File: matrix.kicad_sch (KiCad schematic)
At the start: 2 parts

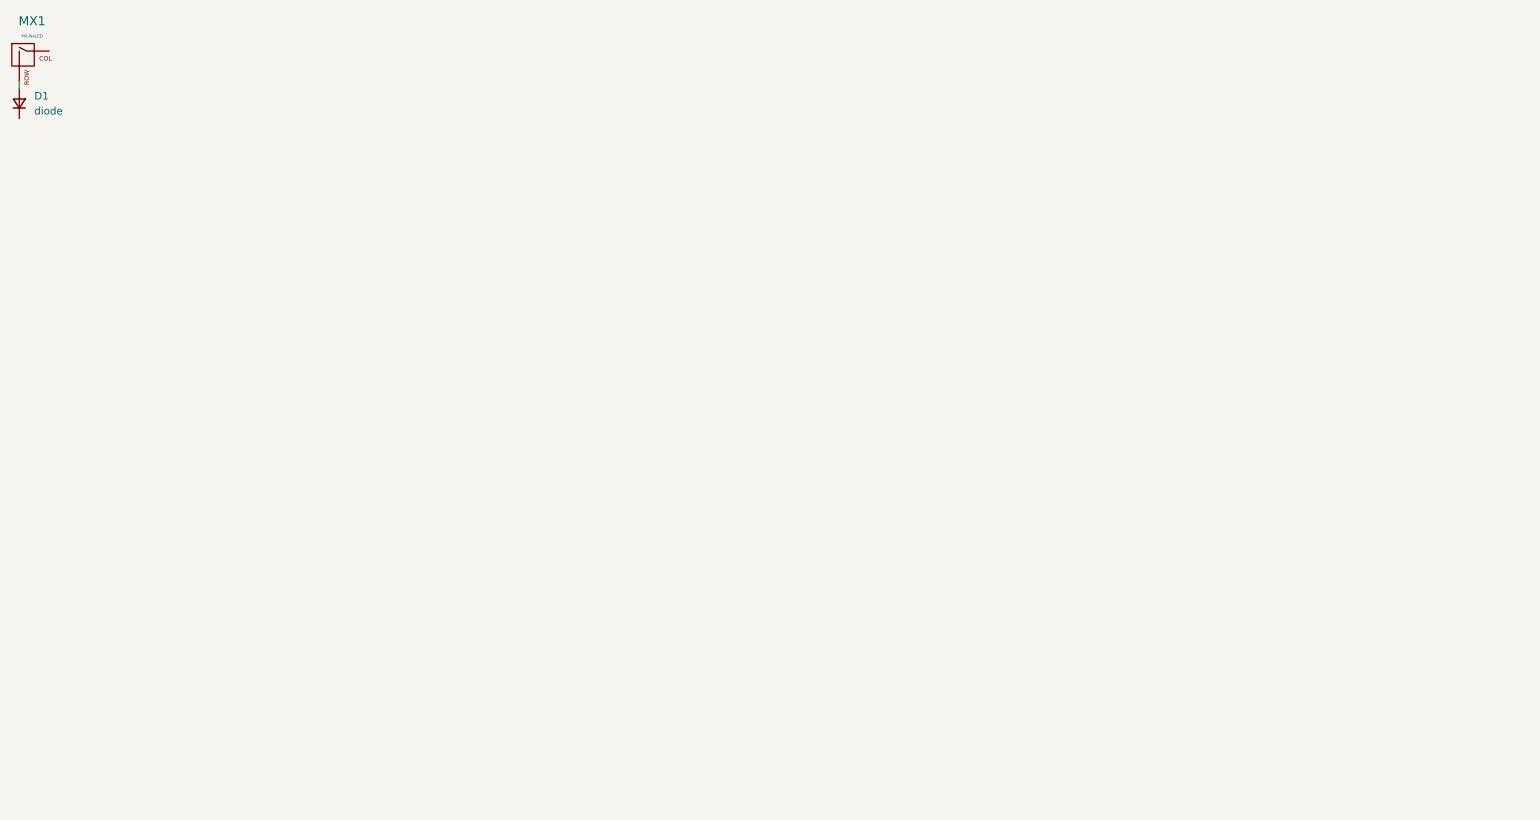
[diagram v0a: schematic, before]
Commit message: First version of schematic, including duplex matrix.
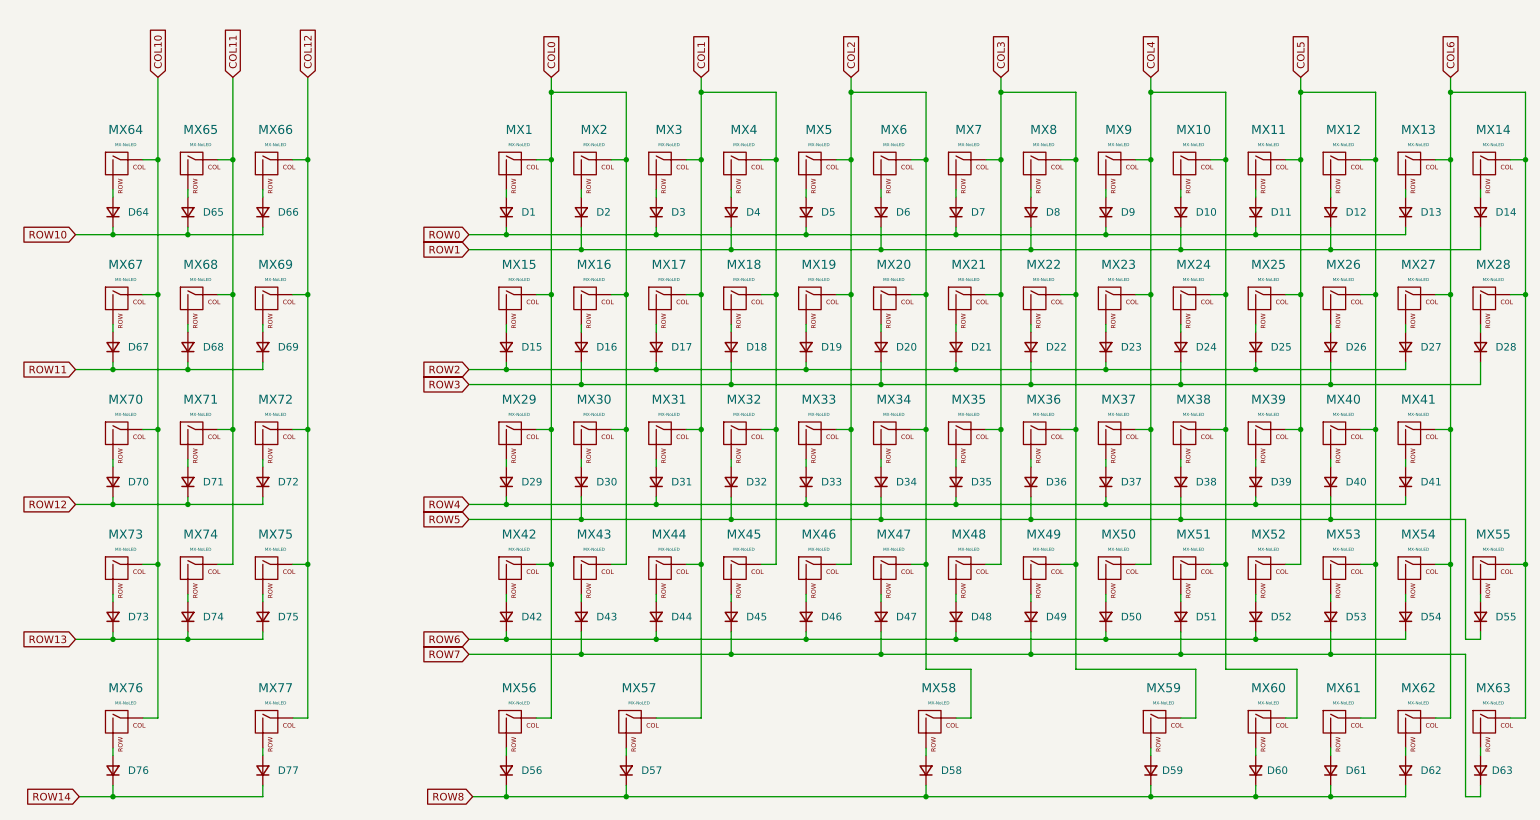
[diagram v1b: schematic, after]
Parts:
- added D10, D11, D12, D13, D14, D15, D16, D17, D18, D19, D2, D20, D21, D22, D23, D24, D25, D26, D27, D28, D29, D3, D30, D31, D32, D33, D34, D35, D36, D37, D38, D39, D4, D40, D41, D42, D43, D44, D45, D46, D47, D48, D49, D5, D50, D51, D52, D53, D54, D55, D56, D57, D58, D59, D6, D60, D61, D62, D63, D64, D65, D66, D67, D68, D69, D7, D70, D71, D72, D73, D74, D75, D76, D77, D8, D9: ~, symbol Device:D_Small
- added MX10, MX11, MX12, MX13, MX14, MX15, MX16, MX17, MX18, MX19, MX2, MX20, MX21, MX22, MX23, MX24, MX25, MX26, MX27, MX28, MX29, MX3, MX30, MX31, MX32, MX33, MX34, MX35, MX36, MX37, MX38, MX39, MX4, MX40, MX41, MX42, MX43, MX44, MX45, MX46, MX47, MX48, MX49, MX5, MX50, MX51, MX52, MX53, MX54, MX55, MX56, MX57, MX58, MX59, MX6, MX60, MX61, MX62, MX63, MX64, MX65, MX66, MX67, MX68, MX69, MX7, MX70, MX71, MX72, MX73, MX74, MX75, MX76, MX77, MX8, MX9: MX-NoLED, symbol MX_Alps_Hybrid:MX-NoLED
- D1: value diode -> ~
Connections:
- net ROW0: now reaches D1.1 (K)
- net ROW0: now also D11.1 (K), D13.1 (K), D3.1 (K), D5.1 (K), D7.1 (K), D9.1 (K)
- net COL0: now reaches MX1.1 (COL)
- net COL0: now also MX15.1 (COL), MX16.1 (COL), MX2.1 (COL), MX29.1 (COL), MX30.1 (COL), MX42.1 (COL), MX43.1 (COL), MX56.1 (COL)
- new net: D65.2 (A), MX65.2 (ROW)
- new net: D21.2 (A), MX21.2 (ROW)
- new net: D74.2 (A), MX74.2 (ROW)
- new net: D17.2 (A), MX17.2 (ROW)
- new net: D15.2 (A), MX15.2 (ROW)
- new net: D49.2 (A), MX49.2 (ROW)
- new net: D51.2 (A), MX51.2 (ROW)
- new net: D20.2 (A), MX20.2 (ROW)
- new net: D18.2 (A), MX18.2 (ROW)
- new net: D26.2 (A), MX26.2 (ROW)
- new net: D64.2 (A), MX64.2 (ROW)
- new net: D24.2 (A), MX24.2 (ROW)
- new net: D67.2 (A), MX67.2 (ROW)
- new net: D34.2 (A), MX34.2 (ROW)
- new net: D25.2 (A), MX25.2 (ROW)
- new net: D59.2 (A), MX59.2 (ROW)
- new net: D73.2 (A), MX73.2 (ROW)
- new net: D44.2 (A), MX44.2 (ROW)
- new net: D39.2 (A), MX39.2 (ROW)
- new net: D37.2 (A), MX37.2 (ROW)
- new net: D10.2 (A), MX10.2 (ROW)
- new net: D48.2 (A), MX48.2 (ROW)
- new net: D76.2 (A), MX76.2 (ROW)
- new net: D68.2 (A), MX68.2 (ROW)
- new net: D33.2 (A), MX33.2 (ROW)
- new net: D66.2 (A), MX66.2 (ROW)
- new net: D22.2 (A), MX22.2 (ROW)
- new net: D5.2 (A), MX5.2 (ROW)
- new net: D3.2 (A), MX3.2 (ROW)
- new net: D6.2 (A), MX6.2 (ROW)
- new net: D63.2 (A), MX63.2 (ROW)
- new net: D40.2 (A), MX40.2 (ROW)
- new net: D50.2 (A), MX50.2 (ROW)
- new net: D19.2 (A), MX19.2 (ROW)
- new net: D31.2 (A), MX31.2 (ROW)
- new net: D52.2 (A), MX52.2 (ROW)
- new net: D28.2 (A), MX28.2 (ROW)
- new net: D47.2 (A), MX47.2 (ROW)
- new net: D30.2 (A), MX30.2 (ROW)
- new net: D53.2 (A), MX53.2 (ROW)
- new net: D13.2 (A), MX13.2 (ROW)
- new net: D42.2 (A), MX42.2 (ROW)
- new net: D72.2 (A), MX72.2 (ROW)
- new net: D12.2 (A), MX12.2 (ROW)
- new net: D2.2 (A), MX2.2 (ROW)
- new net: D23.2 (A), MX23.2 (ROW)
- new net: D56.2 (A), MX56.2 (ROW)
- new net: D9.2 (A), MX9.2 (ROW)
- new net: D14.2 (A), MX14.2 (ROW)
- new net: D11.2 (A), MX11.2 (ROW)
- new net: D8.2 (A), MX8.2 (ROW)
- new net: D35.2 (A), MX35.2 (ROW)
- new net: D29.2 (A), MX29.2 (ROW)
- new net: D45.2 (A), MX45.2 (ROW)
- new net: D46.2 (A), MX46.2 (ROW)
- new net: D7.2 (A), MX7.2 (ROW)
- new net: D16.2 (A), MX16.2 (ROW)
- new net: D57.2 (A), MX57.2 (ROW)
- new net: D58.2 (A), MX58.2 (ROW)
- new net: D36.2 (A), MX36.2 (ROW)
- new net: D75.2 (A), MX75.2 (ROW)
- new net: D41.2 (A), MX41.2 (ROW)
- new net: D54.2 (A), MX54.2 (ROW)
- new net: D60.2 (A), MX60.2 (ROW)
- new net: D32.2 (A), MX32.2 (ROW)
- new net: D55.2 (A), MX55.2 (ROW)
- new net: D69.2 (A), MX69.2 (ROW)
- new net: D4.2 (A), MX4.2 (ROW)
- new net: D43.2 (A), MX43.2 (ROW)
- new net: D71.2 (A), MX71.2 (ROW)
- new net: D62.2 (A), MX62.2 (ROW)
- new net: D61.2 (A), MX61.2 (ROW)
- new net: D77.2 (A), MX77.2 (ROW)
- new net: D38.2 (A), MX38.2 (ROW)
- new net: D70.2 (A), MX70.2 (ROW)
- new net: D27.2 (A), MX27.2 (ROW)
- new net COL1: MX17.1 (COL), MX18.1 (COL), MX3.1 (COL), MX31.1 (COL), MX32.1 (COL), MX4.1 (COL), MX44.1 (COL), MX45.1 (COL), MX57.1 (COL)
- new net COL10: MX64.1 (COL), MX67.1 (COL), MX70.1 (COL), MX73.1 (COL), MX76.1 (COL)
- new net COL11: MX65.1 (COL), MX68.1 (COL), MX71.1 (COL), MX74.1 (COL)
- new net COL12: MX66.1 (COL), MX69.1 (COL), MX72.1 (COL), MX75.1 (COL), MX77.1 (COL)
- new net COL2: MX19.1 (COL), MX20.1 (COL), MX33.1 (COL), MX34.1 (COL), MX46.1 (COL), MX47.1 (COL), MX5.1 (COL), MX58.1 (COL), MX6.1 (COL)
- new net COL3: MX21.1 (COL), MX22.1 (COL), MX35.1 (COL), MX36.1 (COL), MX48.1 (COL), MX49.1 (COL), MX59.1 (COL), MX7.1 (COL), MX8.1 (COL)
- new net COL4: MX10.1 (COL), MX23.1 (COL), MX24.1 (COL), MX37.1 (COL), MX38.1 (COL), MX50.1 (COL), MX51.1 (COL), MX60.1 (COL), MX9.1 (COL)
- new net COL5: MX11.1 (COL), MX12.1 (COL), MX25.1 (COL), MX26.1 (COL), MX39.1 (COL), MX40.1 (COL), MX52.1 (COL), MX53.1 (COL), MX61.1 (COL)
- new net COL6: MX13.1 (COL), MX14.1 (COL), MX27.1 (COL), MX28.1 (COL), MX41.1 (COL), MX54.1 (COL), MX55.1 (COL), MX62.1 (COL), MX63.1 (COL)
- new net ROW1: D10.1 (K), D12.1 (K), D14.1 (K), D2.1 (K), D4.1 (K), D6.1 (K), D8.1 (K)
- new net ROW10: D64.1 (K), D65.1 (K), D66.1 (K)
- new net ROW11: D67.1 (K), D68.1 (K), D69.1 (K)
- new net ROW12: D70.1 (K), D71.1 (K), D72.1 (K)
- new net ROW13: D73.1 (K), D74.1 (K), D75.1 (K)
- new net ROW14: D76.1 (K), D77.1 (K)
- new net ROW2: D15.1 (K), D17.1 (K), D19.1 (K), D21.1 (K), D23.1 (K), D25.1 (K), D27.1 (K)
- new net ROW3: D16.1 (K), D18.1 (K), D20.1 (K), D22.1 (K), D24.1 (K), D26.1 (K), D28.1 (K)
- new net ROW4: D29.1 (K), D31.1 (K), D33.1 (K), D35.1 (K), D37.1 (K), D39.1 (K), D41.1 (K)
- new net ROW5: D30.1 (K), D32.1 (K), D34.1 (K), D36.1 (K), D38.1 (K), D40.1 (K), D55.1 (K)
- new net ROW6: D42.1 (K), D44.1 (K), D46.1 (K), D48.1 (K), D50.1 (K), D52.1 (K), D54.1 (K)
- new net ROW7: D43.1 (K), D45.1 (K), D47.1 (K), D49.1 (K), D51.1 (K), D53.1 (K), D63.1 (K)
- new net ROW8: D56.1 (K), D57.1 (K), D58.1 (K), D59.1 (K), D60.1 (K), D61.1 (K), D62.1 (K)

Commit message: Trying to connect the matrix sheet with the main sheet.
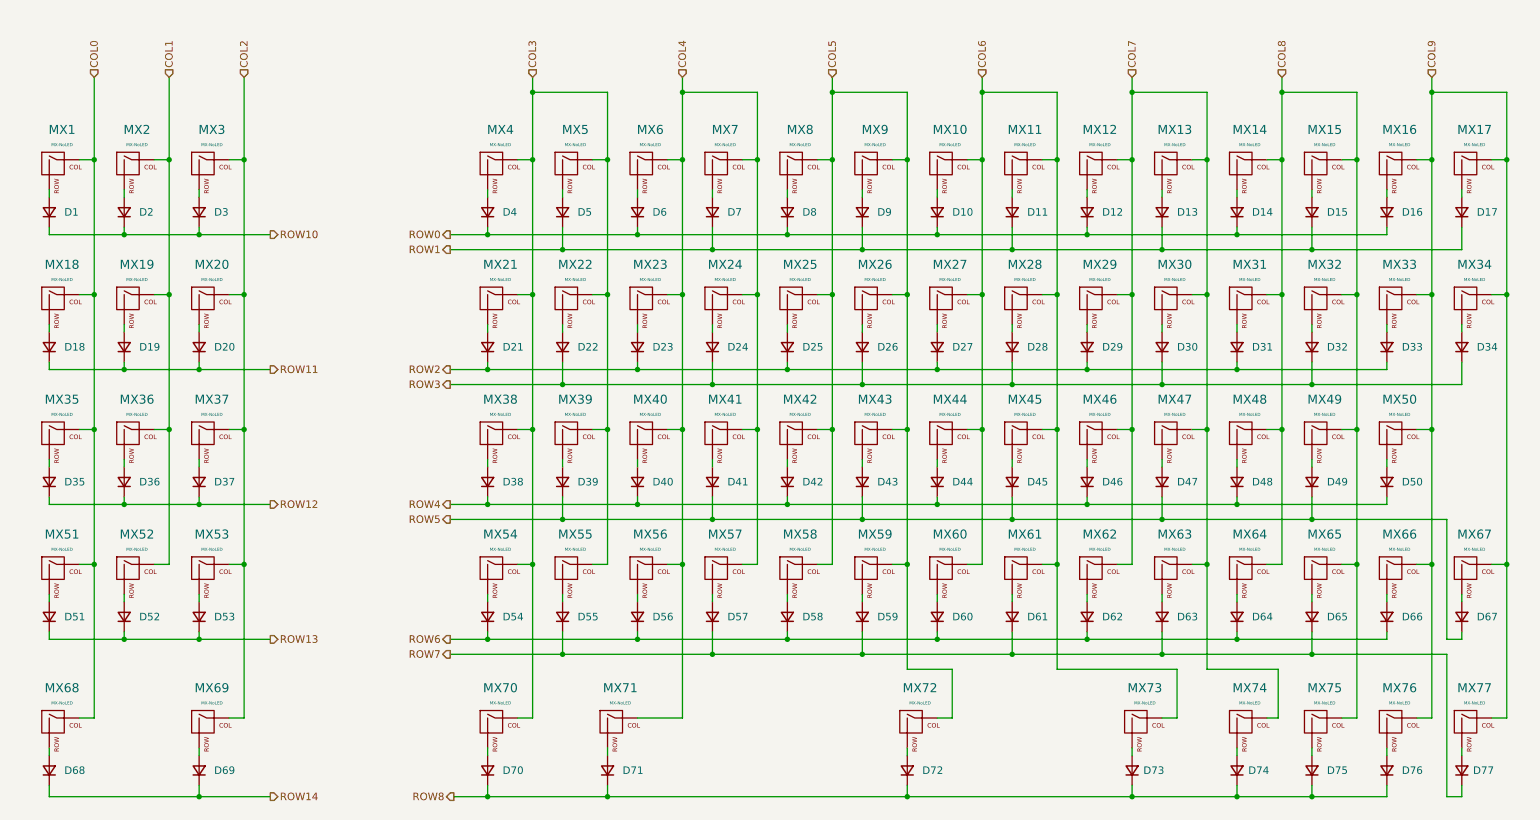
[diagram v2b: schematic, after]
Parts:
- renumbered D64 to D1, D7 to D10, D8 to D11, D9 to D12, D10 to D13, D11 to D14, D12 to D15, D13 to D16, D14 to D17, D67 to D18, D68 to D19, D65 to D2, D69 to D20, D15 to D21, D16 to D22, D17 to D23, D18 to D24, D19 to D25, D20 to D26, D21 to D27, D22 to D28, D23 to D29, D66 to D3, D24 to D30, D25 to D31, D26 to D32, D27 to D33, D28 to D34, D70 to D35, D71 to D36, D72 to D37, D29 to D38, D30 to D39, D1 to D4, D31 to D40, D32 to D41, D33 to D42, D34 to D43, D35 to D44, D36 to D45, D37 to D46, D38 to D47, D39 to D48, D40 to D49, D2 to D5, D41 to D50, D73 to D51, D74 to D52, D75 to D53, D42 to D54, D43 to D55, D44 to D56, D45 to D57, D46 to D58, D47 to D59, D3 to D6, D48 to D60, D49 to D61, D50 to D62, D51 to D63, D52 to D64, D53 to D65, D54 to D66, D55 to D67, D76 to D68, D77 to D69, D4 to D7, D56 to D70, D57 to D71, D58 to D72, D59 to D73, D60 to D74, D61 to D75, D62 to D76, D63 to D77, D5 to D8, D6 to D9, MX64 to MX1, MX7 to MX10, MX8 to MX11, MX9 to MX12, MX10 to MX13, MX11 to MX14, MX12 to MX15, MX13 to MX16, MX14 to MX17, MX67 to MX18, MX68 to MX19, MX65 to MX2, MX69 to MX20, MX15 to MX21, MX16 to MX22, MX17 to MX23, MX18 to MX24, MX19 to MX25, MX20 to MX26, MX21 to MX27, MX22 to MX28, MX23 to MX29, MX66 to MX3, MX24 to MX30, MX25 to MX31, MX26 to MX32, MX27 to MX33, MX28 to MX34, MX70 to MX35, MX71 to MX36, MX72 to MX37, MX29 to MX38, MX30 to MX39, MX1 to MX4, MX31 to MX40, MX32 to MX41, MX33 to MX42, MX34 to MX43, MX35 to MX44, MX36 to MX45, MX37 to MX46, MX38 to MX47, MX39 to MX48, MX40 to MX49, MX2 to MX5, MX41 to MX50, MX73 to MX51, MX74 to MX52, MX75 to MX53, MX42 to MX54, MX43 to MX55, MX44 to MX56, MX45 to MX57, MX46 to MX58, MX47 to MX59, MX3 to MX6, MX48 to MX60, MX49 to MX61, MX50 to MX62, MX51 to MX63, MX52 to MX64, MX53 to MX65, MX54 to MX66, MX55 to MX67, MX76 to MX68, MX77 to MX69, MX4 to MX7, MX56 to MX70, MX57 to MX71, MX58 to MX72, MX59 to MX73, MX60 to MX74, MX61 to MX75, MX62 to MX76, MX63 to MX77, MX5 to MX8, MX6 to MX9
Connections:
- net COL10 is gone; now on net COL0: MX1.1 (COL), MX18.1 (COL), MX35.1 (COL), MX51.1 (COL), MX68.1 (COL)
- net COL11 is gone; now on net COL1: MX19.1 (COL), MX2.1 (COL), MX36.1 (COL), MX52.1 (COL)
- net COL12 is gone; now on net COL2: MX20.1 (COL), MX3.1 (COL), MX37.1 (COL), MX53.1 (COL), MX69.1 (COL)
- net COL0: no longer MX21.1 (COL), MX22.1 (COL), MX38.1 (COL), MX39.1 (COL), MX4.1 (COL), MX5.1 (COL), MX54.1 (COL), MX55.1 (COL), MX70.1 (COL)
- net COL1: no longer MX23.1 (COL), MX24.1 (COL), MX40.1 (COL), MX41.1 (COL), MX56.1 (COL), MX57.1 (COL), MX6.1 (COL), MX7.1 (COL), MX71.1 (COL)
- net COL2: no longer MX25.1 (COL), MX26.1 (COL), MX42.1 (COL), MX43.1 (COL), MX58.1 (COL), MX59.1 (COL), MX72.1 (COL), MX8.1 (COL), MX9.1 (COL)
- net COL3: now also MX21.1 (COL), MX22.1 (COL), MX38.1 (COL), MX39.1 (COL), MX4.1 (COL), MX5.1 (COL), MX54.1 (COL), MX55.1 (COL), MX70.1 (COL); no longer MX10.1 (COL), MX11.1 (COL), MX27.1 (COL), MX28.1 (COL), MX44.1 (COL), MX45.1 (COL), MX60.1 (COL), MX61.1 (COL), MX73.1 (COL)
- net COL4: now also MX23.1 (COL), MX24.1 (COL), MX40.1 (COL), MX41.1 (COL), MX56.1 (COL), MX57.1 (COL), MX6.1 (COL), MX7.1 (COL), MX71.1 (COL); no longer MX12.1 (COL), MX13.1 (COL), MX29.1 (COL), MX30.1 (COL), MX46.1 (COL), MX47.1 (COL), MX62.1 (COL), MX63.1 (COL), MX74.1 (COL)
- net COL5: now also MX25.1 (COL), MX26.1 (COL), MX42.1 (COL), MX43.1 (COL), MX58.1 (COL), MX59.1 (COL), MX72.1 (COL), MX8.1 (COL), MX9.1 (COL); no longer MX14.1 (COL), MX15.1 (COL), MX31.1 (COL), MX32.1 (COL), MX48.1 (COL), MX49.1 (COL), MX64.1 (COL), MX65.1 (COL), MX75.1 (COL)
- net COL6: now also MX10.1 (COL), MX11.1 (COL), MX27.1 (COL), MX28.1 (COL), MX44.1 (COL), MX45.1 (COL), MX60.1 (COL), MX61.1 (COL), MX73.1 (COL); no longer MX16.1 (COL), MX17.1 (COL), MX33.1 (COL), MX34.1 (COL), MX50.1 (COL), MX66.1 (COL), MX67.1 (COL), MX76.1 (COL), MX77.1 (COL)
- new net COL7: MX12.1 (COL), MX13.1 (COL), MX29.1 (COL), MX30.1 (COL), MX46.1 (COL), MX47.1 (COL), MX62.1 (COL), MX63.1 (COL), MX74.1 (COL)
- new net COL8: MX14.1 (COL), MX15.1 (COL), MX31.1 (COL), MX32.1 (COL), MX48.1 (COL), MX49.1 (COL), MX64.1 (COL), MX65.1 (COL), MX75.1 (COL)
- new net COL9: MX16.1 (COL), MX17.1 (COL), MX33.1 (COL), MX34.1 (COL), MX50.1 (COL), MX66.1 (COL), MX67.1 (COL), MX76.1 (COL), MX77.1 (COL)
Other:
- moved on the sheet: D1, D10, D11, D12, D13, D14, D15, D16, D17, D18, D19, D2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
